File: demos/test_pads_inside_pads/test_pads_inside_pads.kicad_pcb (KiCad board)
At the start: 2 copper layers, 4 parts, among them P1 CONN_1, P2 CONN_1, P3 CONN_1, P4 CONN_1

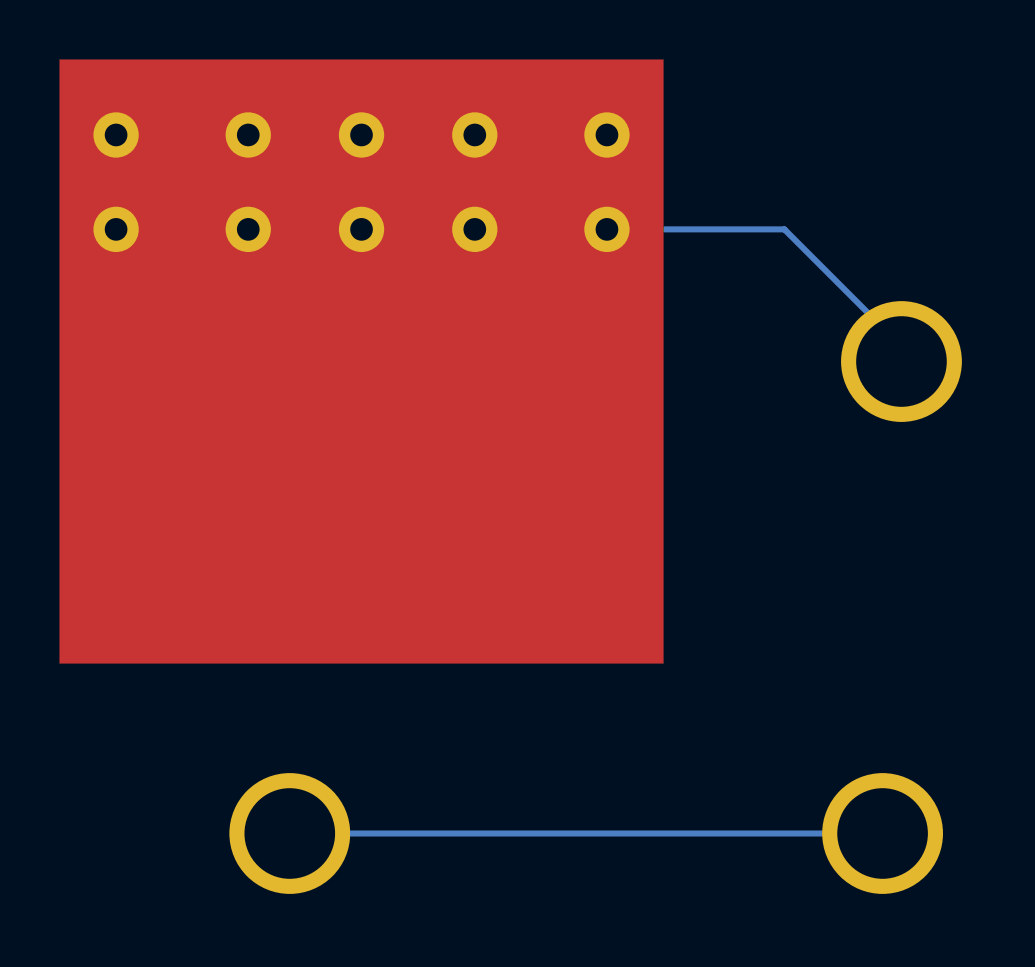
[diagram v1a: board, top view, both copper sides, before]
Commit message: Update old demo board files. Minor code cleaning.
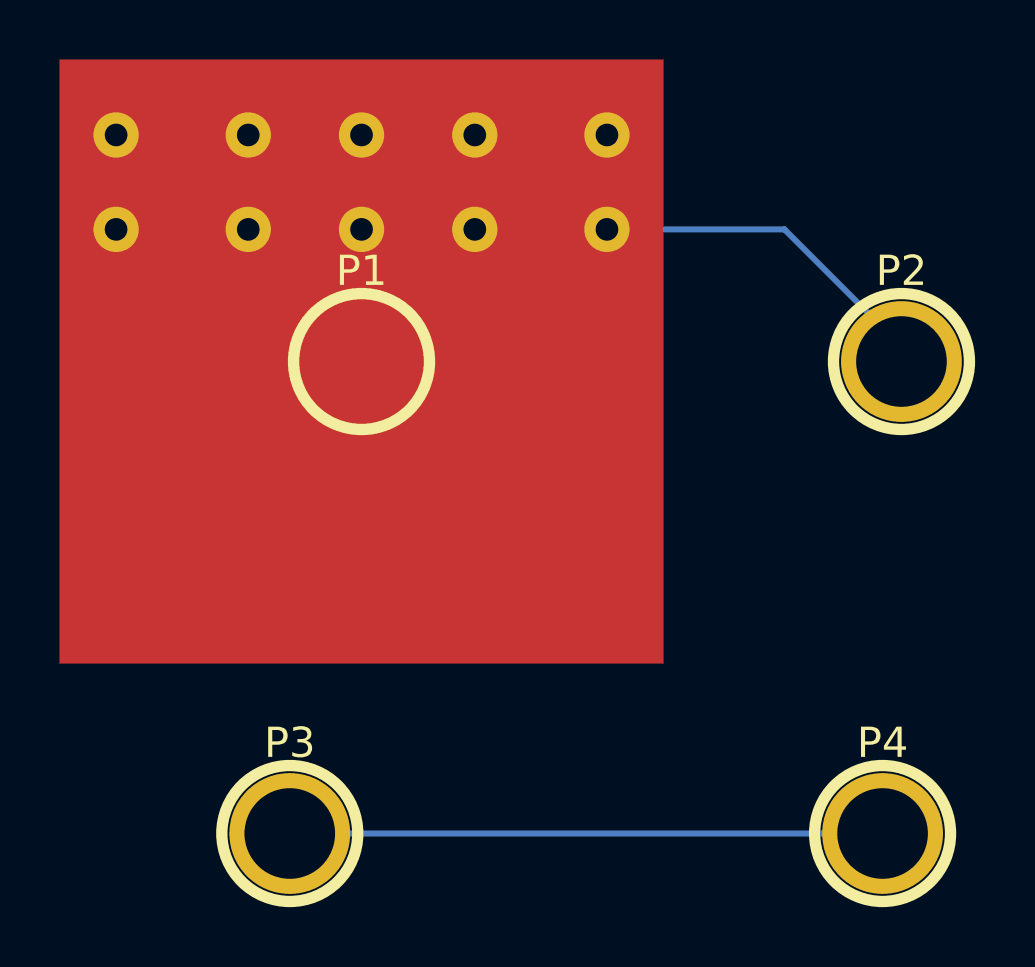
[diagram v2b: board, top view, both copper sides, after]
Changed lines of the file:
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@@
     (15 Dessus signal)
     (0 Dessous signal)
-    (16 Dessous.Adhes user)
-    (17 Dessus.Adhes user)
-    (18 Dessous.Pate user)
-    (19 Dessus.Pate user)
-    (20 Dessous.SilkS user)
-    (21 Dessus.SilkS user)
-    (22 Dessous.Masque user)
-    (23 Dessus.Masque user)
-    (24 Dessin.User user)
+    (16 B.Adhes user)
+    (17 F.Adhes user)
+    (18 B.Paste user)
+    (19 F.Paste user)
+    (20 B.SilkS user)
+    (21 F.SilkS user)
+    (22 B.Mask user)
+    (23 F.Mask user)
+    (24 Dwgs.User user)
     (25 Cmts.User user)
     (26 Eco1.User user)
     (27 Eco2.User user)
-    (28 Contours.Ci user)
+    (28 Edge.Cuts user)
   )
   (setup
@@
     (descr "module 1 pin (ou trou mecanique de percage)")
     (tags DEV)
-    (fp_text reference P1 (at 0 -3.048) (layer Dessus.SilkS)
+    (fp_text reference P1 (at 0 -3.048) (layer F.SilkS)
       (effects (font (size 1.016 1.016) (thickness 0.254)))
     )
-    (fp_text value CONN_1 (at 0 2.794) (layer Dessus.SilkS) hide
+    (fp_text value CONN_1 (at 0 2.794) (layer F.SilkS) hide
       (effects (font (size 1.016 1.016) (thickness 0.254)))
     )
-    (fp_circle (center 0 0) (end 0 -2.286) (layer Dessus.SilkS) (width 0.381))
+    (fp_circle (center 0 0) (end 0 -2.286) (layer F.SilkS) (width 0.381))
     (pad 1 smd rect (at 0 0) (size 20.32 20.32)
-      (layers Dessus Dessus.Pate Dessus.Masque)
+      (layers Dessus F.Paste F.Mask)
       (net 2 /NET2)
     )
     (pad 1 thru_hole circle (at -8.255 -7.62) (size 1.524 1.524) (drill 0.762)
-      (layers *.Cu *.Mask Dessus.SilkS)
+      (layers *.Cu *.Mask F.SilkS)
       (net 2 /NET2)
     )
     (pad 1 thru_hole circle (at -3.81 -7.62) (size 1.524 1.524) (drill 0.762)
-      (layers *.Cu *.Mask Dessus.SilkS)
+      (layers *.Cu *.Mask F.SilkS)
       (net 2 /NET2)
     )
     (pad 1 thru_hole circle (at 0 -7.62) (size 1.524 1.524) (drill 0.762)
-      (layers *.Cu *.Mask Dessus.SilkS)
+      (layers *.Cu *.Mask F.SilkS)
       (net 2 /NET2)
     )
     (pad 1 thru_hole circle (at 3.81 -7.62) (size 1.524 1.524) (drill 0.762)
-      (layers *.Cu *.Mask Dessus.SilkS)
+      (layers *.Cu *.Mask F.SilkS)
       (net 2 /NET2)
     )
     (pad 1 thru_hole circle (at 8.255 -7.62) (size 1.524 1.524) (drill 0.762)
-      (layers *.Cu *.Mask Dessus.SilkS)
+      (layers *.Cu *.Mask F.SilkS)
       (net 2 /NET2)
     )
     (pad 1 thru_hole circle (at 8.255 -4.445) (size 1.524 1.524) (drill 0.762)
-      (layers *.Cu *.Mask Dessus.SilkS)
+      (layers *.Cu *.Mask F.SilkS)
       (net 2 /NET2)
     )
     (pad 1 thru_hole circle (at 3.81 -4.445) (size 1.524 1.524) (drill 0.762)
-      (layers *.Cu *.Mask Dessus.SilkS)
+      (layers *.Cu *.Mask F.SilkS)
       (net 2 /NET2)
     )
     (pad 1 thru_hole circle (at 0 -4.445) (size 1.524 1.524) (drill 0.762)
-      (layers *.Cu *.Mask Dessus.SilkS)
+      (layers *.Cu *.Mask F.SilkS)
       (net 2 /NET2)
     )
     (pad 1 thru_hole circle (at -3.81 -4.445) (size 1.524 1.524) (drill 0.762)
-      (layers *.Cu *.Mask Dessus.SilkS)
+      (layers *.Cu *.Mask F.SilkS)
       (net 2 /NET2)
     )
     (pad 1 thru_hole circle (at -8.255 -4.445) (size 1.524 1.524) (drill 0.762)
-      (layers *.Cu *.Mask Dessus.SilkS)
+      (layers *.Cu *.Mask F.SilkS)
       (net 2 /NET2)
     )
@@
     (descr "module 1 pin (ou trou mecanique de percage)")
     (tags DEV)
-    (fp_text reference P2 (at 0 -3.048) (layer Dessus.SilkS)
+    (fp_text reference P2 (at 0 -3.048) (layer F.SilkS)
       (effects (font (size 1.016 1.016) (thickness 0.254)))
     )
-    (fp_text value CONN_1 (at 0 2.794) (layer Dessus.SilkS) hide
+    (fp_text value CONN_1 (at 0 2.794) (layer F.SilkS) hide
       (effects (font (size 1.016 1.016) (thickness 0.254)))
     )
-    (fp_circle (center 0 0) (end 0 -2.286) (layer Dessus.SilkS) (width 0.381))
+    (fp_circle (center 0 0) (end 0 -2.286) (layer F.SilkS) (width 0.381))
     (pad 1 thru_hole circle (at 0 0) (size 4.064 4.064) (drill 3.048)
-      (layers *.Cu *.Mask Dessus.SilkS)
+      (layers *.Cu *.Mask F.SilkS)
       (net 2 /NET2)
     )
@@
     (descr "module 1 pin (ou trou mecanique de percage)")
     (tags DEV)
-    (fp_text reference P3 (at 0 -3.048) (layer Dessus.SilkS)
+    (fp_text reference P3 (at 0 -3.048) (layer F.SilkS)
       (effects (font (size 1.016 1.016) (thickness 0.254)))
     )
-    (fp_text value CONN_1 (at 0 2.794) (layer Dessus.SilkS) hide
+    (fp_text value CONN_1 (at 0 2.794) (layer F.SilkS) hide
       (effects (font (size 1.016 1.016) (thickness 0.254)))
     )
-    (fp_circle (center 0 0) (end 0 -2.286) (layer Dessus.SilkS) (width 0.381))
+    (fp_circle (center 0 0) (end 0 -2.286) (layer F.SilkS) (width 0.381))
     (pad 1 thru_hole circle (at 0 0) (size 4.064 4.064) (drill 3.048)
-      (layers *.Cu *.Mask Dessus.SilkS)
+      (layers *.Cu *.Mask F.SilkS)
       (net 1 /NET1)
     )
@@
     (descr "module 1 pin (ou trou mecanique de percage)")
     (tags DEV)
-    (fp_text reference P4 (at 0 -3.048) (layer Dessus.SilkS)
+    (fp_text reference P4 (at 0 -3.048) (layer F.SilkS)
       (effects (font (size 1.016 1.016) (thickness 0.254)))
     )
-    (fp_text value CONN_1 (at 0 2.794) (layer Dessus.SilkS) hide
+    (fp_text value CONN_1 (at 0 2.794) (layer F.SilkS) hide
       (effects (font (size 1.016 1.016) (thickness 0.254)))
     )
-    (fp_circle (center 0 0) (end 0 -2.286) (layer Dessus.SilkS) (width 0.381))
+    (fp_circle (center 0 0) (end 0 -2.286) (layer F.SilkS) (width 0.381))
     (pad 1 thru_hole circle (at 0 0) (size 4.064 4.064) (drill 3.048)
-      (layers *.Cu *.Mask Dessus.SilkS)
+      (layers *.Cu *.Mask F.SilkS)
       (net 1 /NET1)
       (die_length 7.62)
